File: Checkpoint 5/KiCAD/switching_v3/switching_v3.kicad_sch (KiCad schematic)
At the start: 60 parts, among them J1 Conn_01x02, J2 TP_BATT, J3 Conn_01x02, J4 TP_GND, J5 TP_GND, Q1 IRF740, Q2 IRF740, U1 LM7809_TO220, U2 LM393, U3 IR2104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

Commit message: correción PCB
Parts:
- removed JP1: Jumper_2_Bridged, Connector_PinHeader_2.54mm:PinHeader_1x02_P2.54mm_Vertical, symbol Jumper:Jumper_2_Bridged
- removed JP10: TP_Bootstrap, Connector_PinHeader_2.54mm:PinHeader_1x02_P2.54mm_Vertical, symbol Jumper:Jumper_2_Bridged
- removed JP2: TP_Cuadrada, Connector_PinHeader_2.54mm:PinHeader_1x02_P2.54mm_Vertical, symbol Jumper:Jumper_2_Bridged
- removed JP3: TP_Traing, Connector_PinHeader_2.54mm:PinHeader_1x02_P2.54mm_Vertical, symbol Jumper:Jumper_2_Bridged
- removed TP10: TP_Vo, Connector_PinHeader_2.54mm:PinHeader_1x01_P2.54mm_Vertical, symbol Connector:TestPoint
- removed U5: TL071, Package_DIP:DIP-8_W7.62mm_LongPads, symbol Amplifier_Operational:TL071
- added J6: TP_Cuad, Connector_PinHeader_2.54mm:PinHeader_1x02_P2.54mm_Vertical, symbol Connector:Conn_01x02_Pin
- added J7: TP_Triang, Connector_PinHeader_2.54mm:PinHeader_1x02_P2.54mm_Vertical, symbol Connector:Conn_01x02_Pin
- added J8: TP_Bootstrap, Connector_PinHeader_2.54mm:PinHeader_1x02_P2.54mm_Vertical, symbol Connector:Conn_01x02_Pin
- added J9: TP_Vo, Connector_PinHeader_2.54mm:PinHeader_1x02_P2.54mm_Vertical, symbol Connector:Conn_01x02_Pin
- added R12, R4: 470k, Resistor_THT:R_Axial_DIN0207_L6.3mm_D2.5mm_P7.62mm_Horizontal, symbol Device:R
- added U6: TL072, Package_DIP:DIP-8_W7.62mm_Socket_LongPads, symbol Amplifier_Operational:TL072
- C9: footprint Capacitor_THT:C_Disc_D5.0mm_W2.5mm_P2.50mm -> Capacitor_THT:C_Disc_D8.0mm_W2.5mm_P5.00mm
- U3: footprint Package_DIP:DIP-8_W7.62mm_LongPads -> Package_DIP:DIP-8_W7.62mm_Socket_LongPads
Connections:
- net +9V: now also D4.2 (A), R4.1, U6.8 (V+); no longer R10.1
- net Cuad: now also R5.1, J6.1 (Pin_1), J6.2 (Pin_2)
- net GND: now also R12.2, U6.4 (V-)
- net Triang: now also U2.6 (-), J7.1 (Pin_1), J7.2 (Pin_2)
- net Vo: now also Rc3.2, J9.1 (Pin_1), J9.2 (Pin_2); no longer Cc2.2
- net Vref: now also U4.1, U4.2 (-)
- net at D4.1 (K): now also R10.1
- net at C10.1, U3.8 (VB): now also R10.2, J8.1 (Pin_1), J8.2 (Pin_2)
- net at Cc3.1, JP7.2 (B), Rc2.1: now also U6.1
- net at Cc1.2, Cc3.2, R11.1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: now also Cc2.1, U6.2 (-); no longer Rc3.1
- new net: R12.1, R4.2, U6.5 (+)
- new net: Cc2.2, Rc3.1
- new net Vref_comp: U6.3 (+), U6.6 (-), U6.7
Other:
- moved on the sheet: C14, Cc1, Cc2, Cc3, D4, J4, JP7, R10, R11, R15, Rc1, Rc2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

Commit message: lista de materiales
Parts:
- R1, R2: value 560k -> 1Meg
- R10, R7, R8: value 1 -> 10
- R12, R4: value 470k -> 1Meg
- R3: value 4k7 -> 5k1
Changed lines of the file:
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@@
 			)
 		)
-		(property "Value" "470k"
+		(property "Value" "1Meg"
 			(at 264.16 129.5399 0)
 			(show_name no)
@@
 			)
 		)
-		(property "Value" "470k"
+		(property "Value" "1Meg"
 			(at 264.16 149.8599 0)
 			(show_name no)
@@
 			)
 		)
-		(property "Value" "1"
+		(property "Value" "10"
 			(at 59.436 81.28 90)
 			(show_name no)
@@
 			)
 		)
-		(property "Value" "1"
+		(property "Value" "10"
 			(at 72.39 50.546 90)
 			(show_name no)
@@
 			)
 		)
-		(property "Value" "4k7"
+		(property "Value" "5k1"
 			(at 231.14 69.8499 0)
 			(show_name no)
@@
 			)
 		)
-		(property "Value" "560k"
+		(property "Value" "1Meg"
 			(at 29.21 116.8399 0)
 			(show_name no)
@@
 			)
 		)
-		(property "Value" "560k"
+		(property "Value" "1Meg"
 			(at 29.21 137.1599 0)
 			(show_name no)
@@
 			)
 		)
-		(property "Value" "1"
+		(property "Value" "10"
 			(at 59.69 68.58 90)
 			(show_name no)

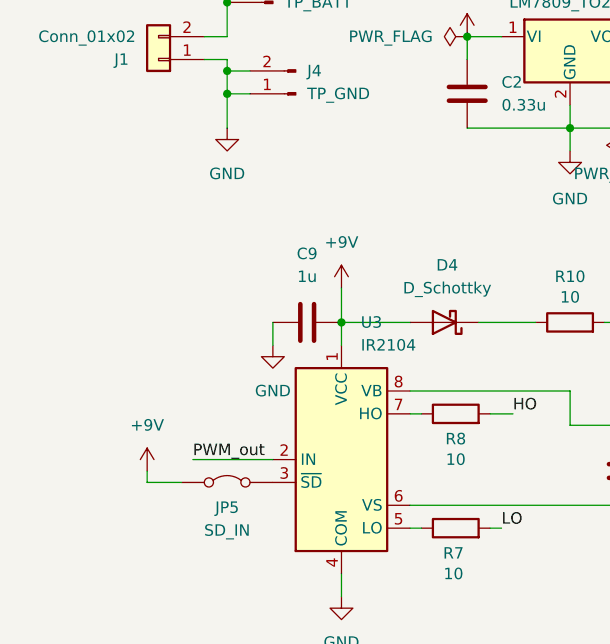
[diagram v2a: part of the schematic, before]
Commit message: agregué el LM7810
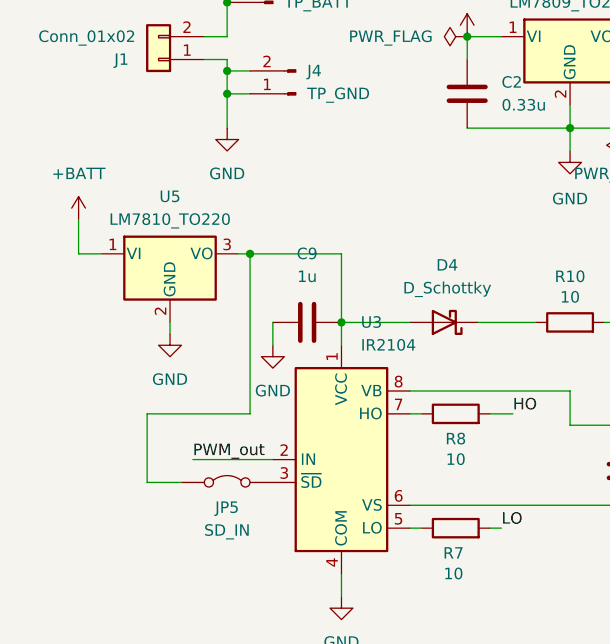
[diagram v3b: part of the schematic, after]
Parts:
- added U5: LM7810_TO220, Package_TO_SOT_THT:TO-220-3_Vertical, symbol Regulator_Linear:LM7810_TO220
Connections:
- net +9V: no longer C9.2, D4.2 (A), JP5.1 (A), U3.1 (VCC)
- net +BATT: now also U5.1 (VI)
- net GND: now also U5.2 (GND)
- new net: C9.2, D4.2 (A), JP5.1 (A), U3.1 (VCC), U5.3 (VO)

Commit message: commit final
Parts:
- Cc1: value 22n -> 30n
- Cc3: value 5.6n -> 4.7n
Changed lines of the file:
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@@
 			)
 		)
-		(property "Value" "22n"
+		(property "Value" "30n"
 			(at 176.53 115.57 90)
 			(show_name no)
@@
 			)
 		)
-		(property "Value" "5.6n"
+		(property "Value" "4.7n"
 			(at 171.45 101.6 90)
 			(show_name no)
